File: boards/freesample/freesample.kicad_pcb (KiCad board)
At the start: 8 copper layers, 576 parts, among them J1 SMA, J10 XILINX_JTAG, J11 SMA, J12 SMA, J13 SMA, J14 SMA, J15 SMA, J16 SMA, J17 SMA, J18 SMA, J19 JUMPER, J2 BARREL, J20 JUMPER, J21 JUMPER, J22 SMA, J23 SMA, J24 SMA, J25 SMA, J26 PMOD_HOST, J3 SMA, J4 SMA, J5 SMA, J6 XILINX_JTAG, J7 CONN_INTEGRALSTICK_FPGA_HOST, J8 CONN_INTEGRALSTICK_MCU_HOST, J9 0826-1G1T-23-F, M1 TRACEPAD, M2 LOGO1, M3 LOGO2, M4 LOGO3, M5 LOGO4, M6 LOGO5, M7 LOGO6, Q1 SSM6N58NU, U1 HMC675LP3E, U10 PI6C59S6005, U11 PI6C59S6005, U12 PI6C59S6005, U13 SIP32408, U14 LMK04806, U15 ASG-D-V-A-125.000MHZ, U16 HMC856, U17 NB6L295, U18 PI6C59S6005, U19 NB7V52MMNG, U2 HMC675LP3E, U20 NB7V52MMNG, U21 NB7V52MMNG, U22 PI6C59S6005, U26 MCP1755ST-5002E/MC, U27 LM27761, U28 ADP1763Z-1.0, U29 ADP1763Z-1.0, U3 PI6C59S6005, U30 OKL-T/3-W12P-C, U31 ADP1741, U32 OKL-T/3-W12P-C, U33 ADP1741, U34 ADP1741, U35 OKL-T/3-W12P-C, U36 OKL-T/3-W12P-C, U37 LM27761, U38 OKL-T/3-W12P-C, U39 LM27761, U4 LTC2664CUH-16#PBF, U40 DS25BR150, U41 DS25BR150, U42 ADP1741, U43 ADP1741, U5 TLK10232, U6 LMK61PD0A2, U7 PI6C59S6005, U8 HMC675LP3E, U9 HMC675LP3E

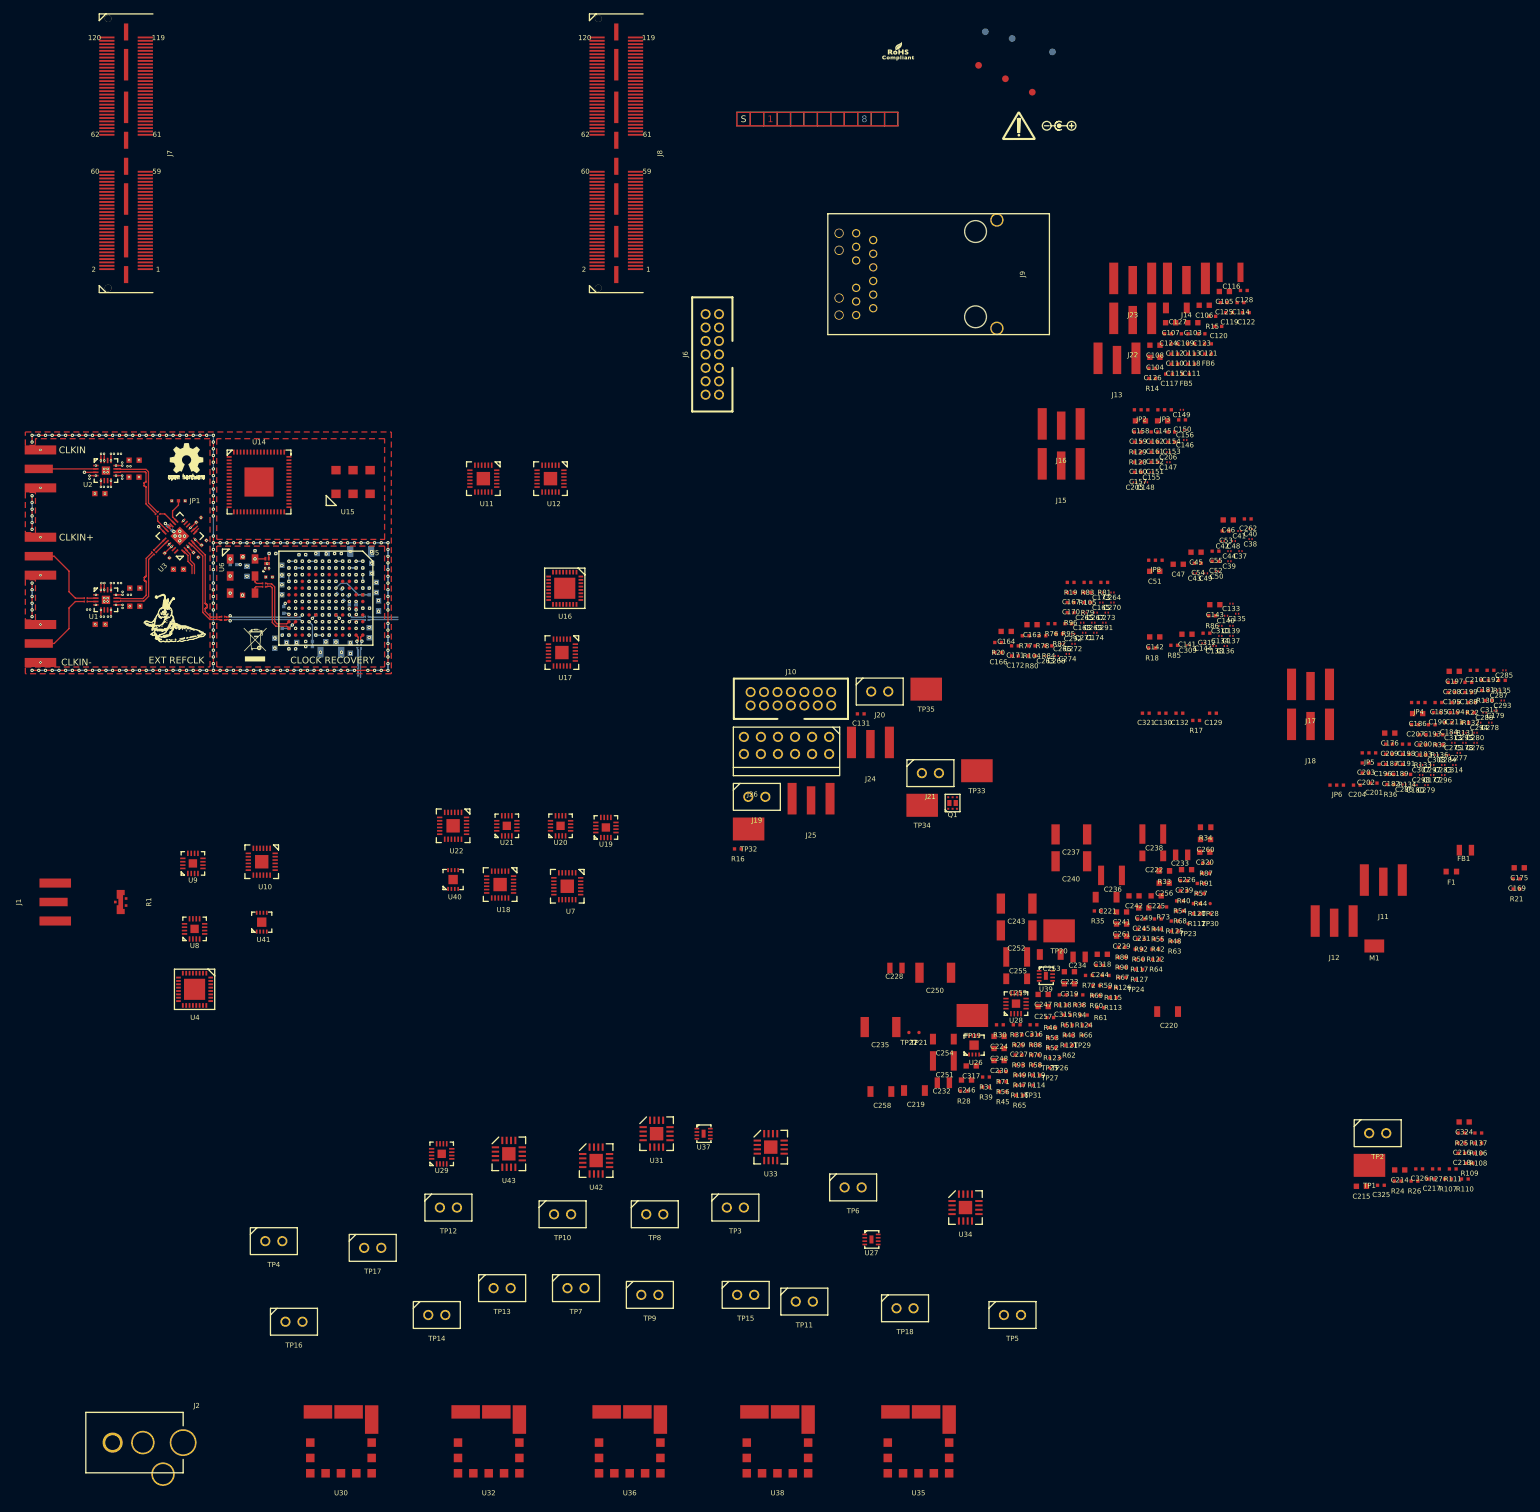
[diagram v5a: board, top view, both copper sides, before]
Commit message: Swapped clock inputs to TLK10232 to reduce via count. Began PLL layout.
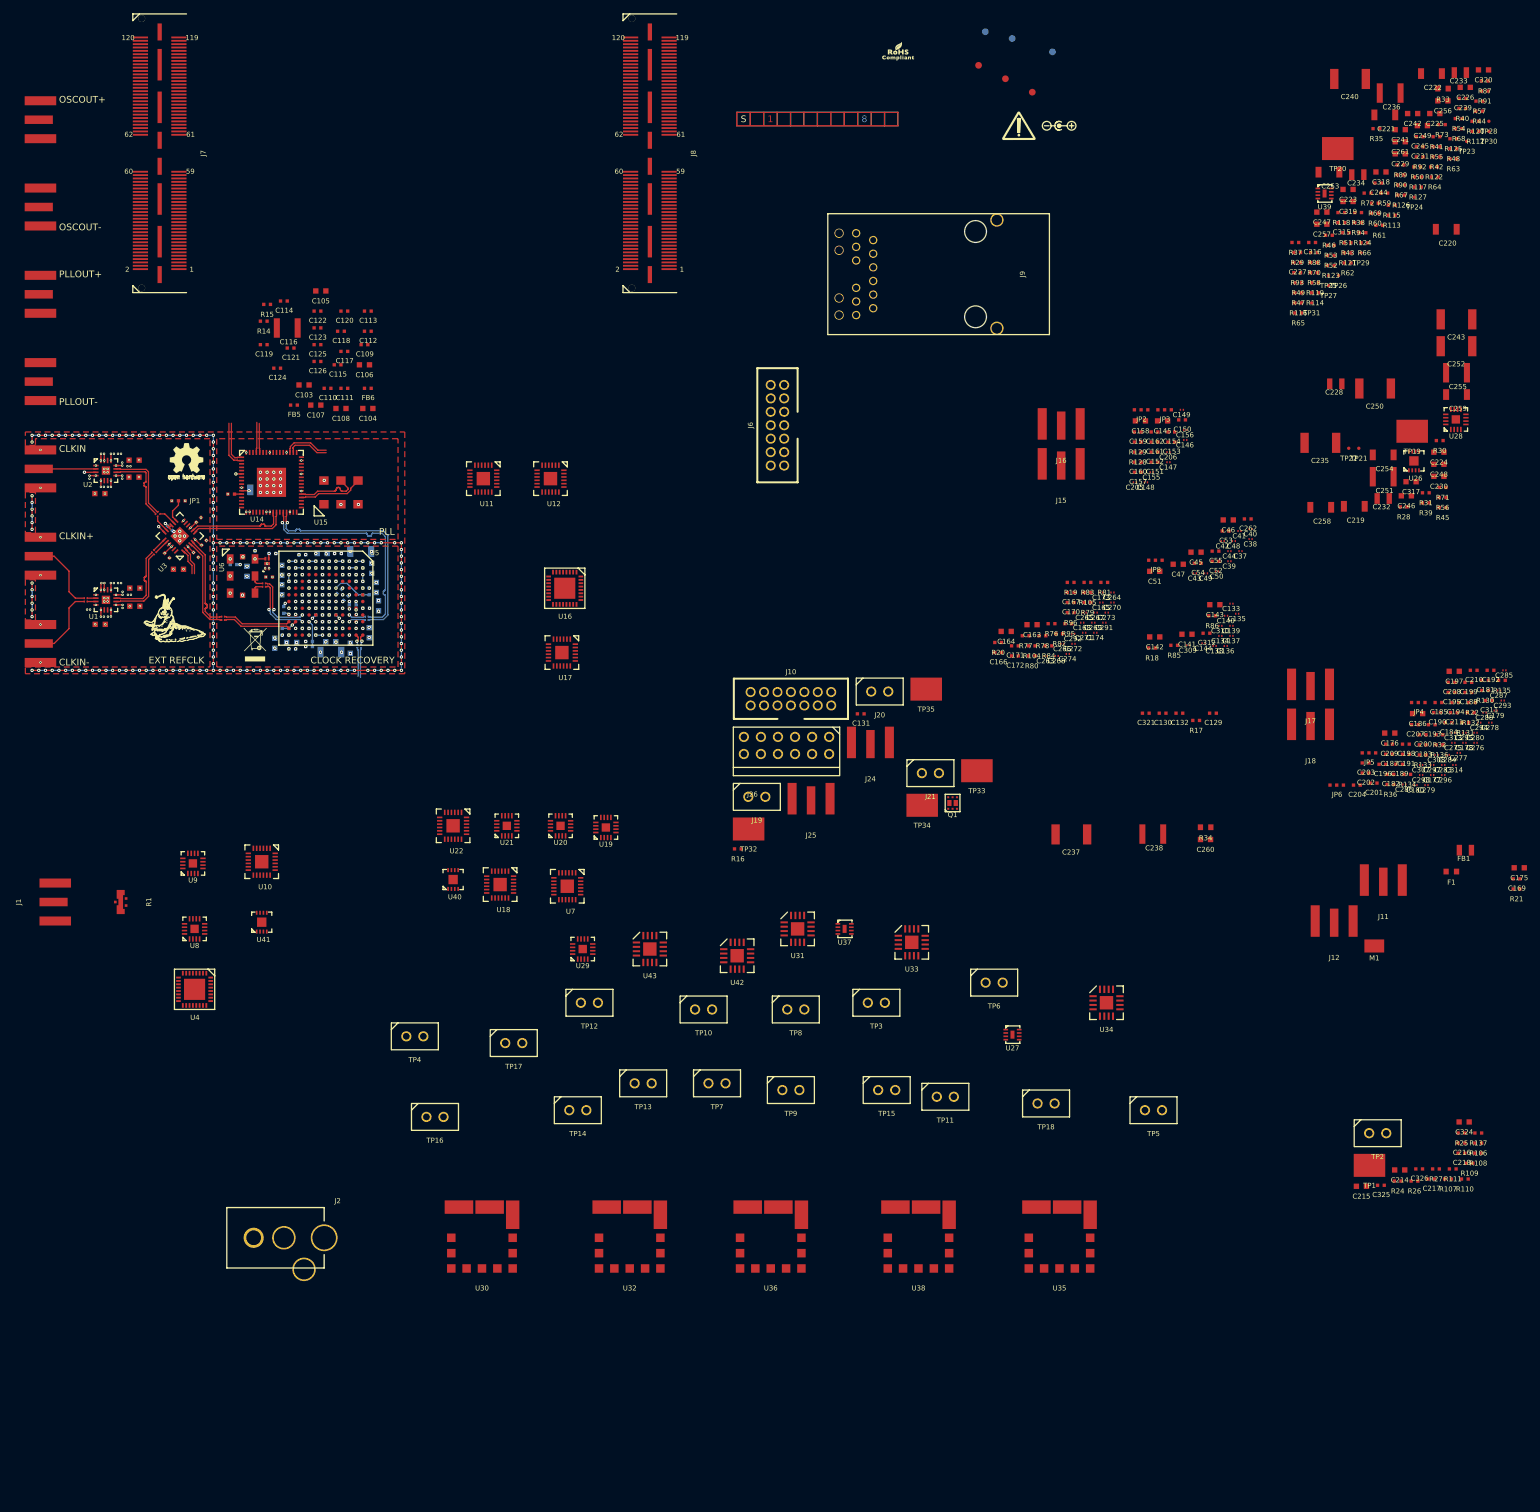
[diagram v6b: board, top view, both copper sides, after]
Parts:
- C127: moved to B.Cu
- moved J14 173.5 mm to (15.9, 112.0), turned to 270 degrees
- moved J22 168.1 mm to (15.9, 73.0), turned to 270 degrees
- moved J23 165.5 mm to (15.9, 86.0), turned to 270 degrees
- moved J13 163.1 mm to (15.9, 99.0), turned to 270 degrees
- moved C128 153.8 mm to (46.6, 128.8)
- moved C119 143.8 mm to (51.5, 106.5)
- moved C114 142.5 mm to (54.5, 100.0)
- moved R15 140.8 mm to (52.0, 100.5)
- moved C116 140.6 mm to (55.0, 104.0)
- moved C127 139.0 mm to (51.0, 128.1), turned to 180 degrees
- moved C122 138.3 mm to (59.5, 101.5)
- moved C121 136.6 mm to (55.5, 107.0)
- moved C125 135.1 mm to (59.5, 106.5)
- moved C105 134.6 mm to (60.0, 98.5)
- moved FB5 132.9 mm to (56.0, 115.5)
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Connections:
- U14 pad 1: /Sample clock muxing/PLL_SAMPCLK_P -> /PLL/PLLOUT_P
- U14 pad 13: /FPGACLK_P -> (no net)
- U14 pad 14: /FPGACLK_N -> (no net)
- U14 pad 19: /PLL/PLLOUT_P -> (no net)
- U14 pad 2: /Sample clock muxing/PLL_SAMPCLK_N -> /PLL/PLLOUT_N
- U14 pad 20: /PLL/PLLOUT_N -> (no net)
- U14 pad 50: (no net) -> /Sample clock muxing/PLL_SAMPCLK_N
- U14 pad 51: (no net) -> /Sample clock muxing/PLL_SAMPCLK_P
- U14 pad 60: (no net) -> /FPGACLK_N
- U14 pad 61: (no net) -> /FPGACLK_P
- U5 pad K10: /CDR/SRC1_AC_N -> /CDR/SRC0_AC_N
- U5 pad K9: /CDR/SRC1_AC_P -> /CDR/SRC0_AC_P
- U5 pad M10: /CDR/SRC0_AC_P -> /CDR/SRC1_AC_P
- U5 pad M11: /CDR/SRC0_AC_N -> /CDR/SRC1_AC_N
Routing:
- net /GND: track 431.5 -> 469.3 mm, vias 289 -> 312
- net /3V3_PLL: track 20.2 -> 56.5 mm, vias 2 -> 15
- net /PLL/CDRCLK_N: track 4.46 -> 33.5 mm, vias 0 -> 1
- net /PLL/CDRCLK_P: track 4.46 -> 33.5 mm, vias 0 -> 1
- net /PLL/EXTCLK_N: track 0.79 -> 14.5 mm
- net /PLL/EXTCLK_P: track 0.94 -> 14.5 mm
- net /PLL/PLL1_CLK_N: track 0.00 -> 9.71 mm
- net /PLL/PLL1_CLK_P: track 0.00 -> 9.68 mm
- net /PLL/PLLOUT_N: track 0.00 -> 6.99 mm
- net /Sample clock muxing/PLL_SAMPCLK_P: track 0.00 -> 6.92 mm
- net /OSC_PWR_EN: track 7.95 -> 1.15 mm
- net /PLL/PLLOUT_P: track 0.00 -> 6.38 mm
- net /Sample clock muxing/PLL_SAMPCLK_N: track 0.00 -> 6.32 mm
- net /FPGACLK_P: track 0.00 -> 4.50 mm
- net /FPGACLK_N: track 0.00 -> 4.35 mm
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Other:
- board text added: "OSCOUT+"
- board text added: "OSCOUT-"
- board text added: "PLL"
- board text added: "PLLOUT+"
- board text added: "PLLOUT-"

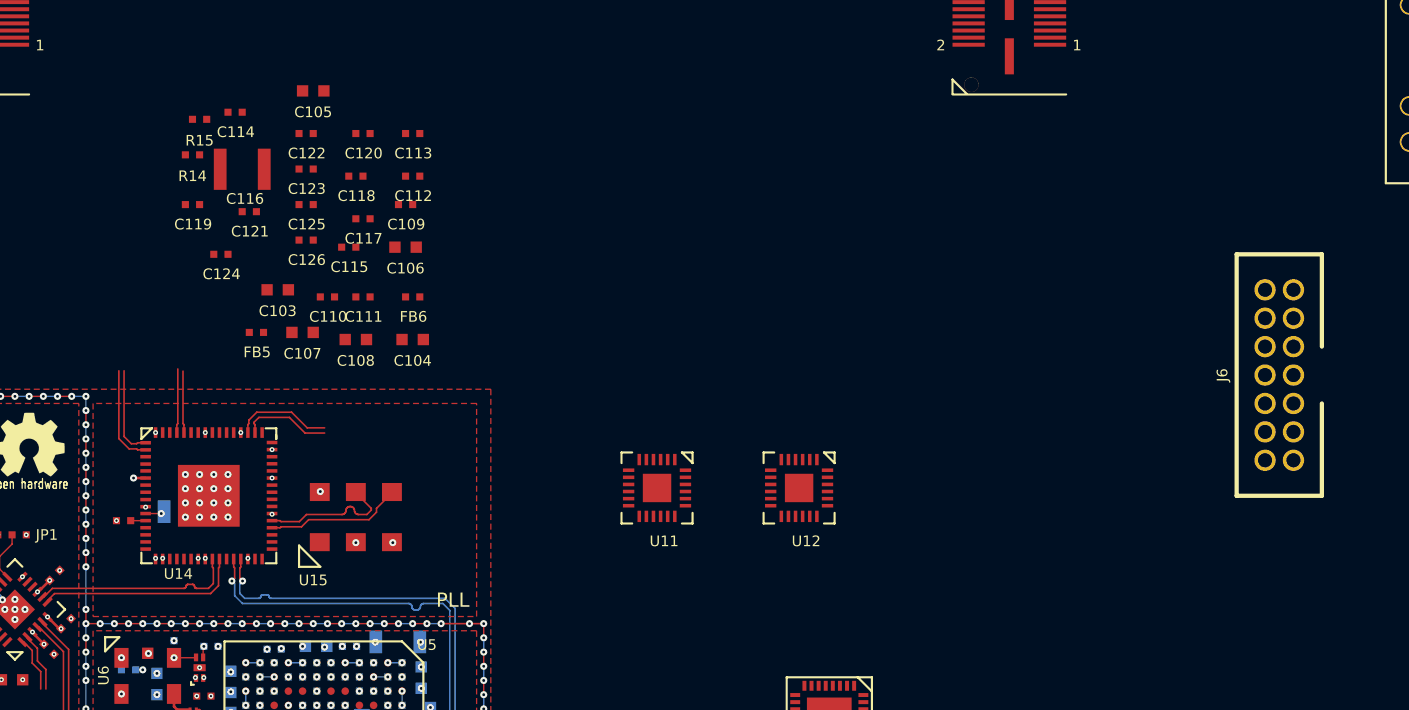
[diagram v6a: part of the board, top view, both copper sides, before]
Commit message: Finished initial PLL layout
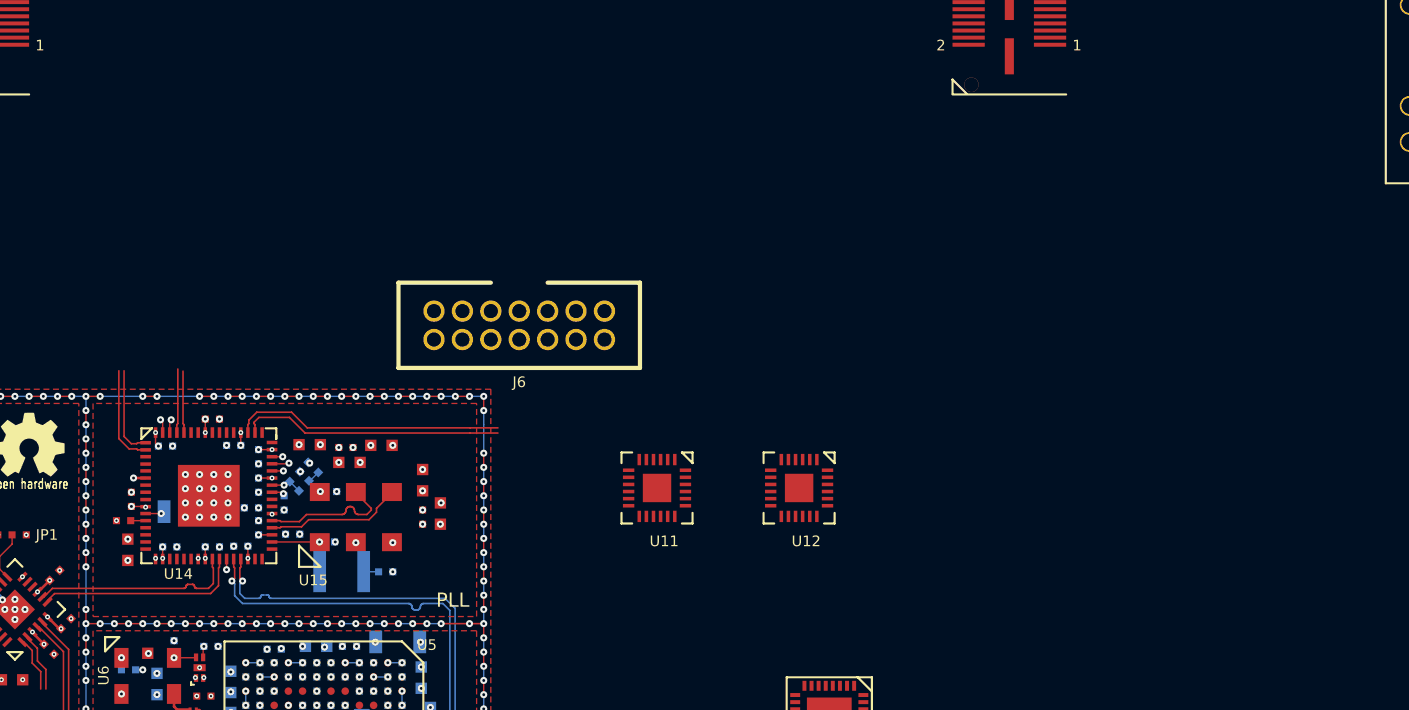
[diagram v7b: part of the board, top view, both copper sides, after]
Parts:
- C109, C110, C111, C112, C113, C114, C115, C116, C118, C119, C120, C121, C122, C123, C124, C126, R14, R15: moved to B.Cu
- moved J6 53.6 mm to (74.5, 115.0), turned to 180 degrees
- moved C105 34.8 mm to (47.0, 130.8), turned to 90 degrees
- moved R14 32.3 mm to (65.1, 132.3)
- moved C113 32.3 mm to (52.9, 130.6)
- moved C112 31.2 mm to (49.9, 130.6)
- moved C114 30.9 mm to (61.0, 130.2)
- moved C122 29.4 mm to (54.9, 130.6), turned to 180 degrees
- moved C116 29.2 mm to (62.0, 132.3)
- moved R15 25.8 mm to (60.0, 125.0), turned to 135 degrees
- moved C109 24.5 mm to (58.5, 129.7)
- moved C118 24.5 mm to (55.6, 127.8), turned to 180 degrees
- moved C125 24.1 mm to (47.2, 127.2), turned to 90 degrees
- moved C120 23.9 mm to (56.1, 124.2), turned to 270 degrees
- moved C123 21.9 mm to (49.6, 123.5)
- moved C119 20.5 mm to (58.7, 125.7), turned to 45 degrees
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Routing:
- net /GND: track 469.3 -> 565.4 mm, vias 312 -> 373
- net /3V3_PLL: track 56.5 -> 93.6 mm, vias 15 -> 32
- net /OSC_PWR_EN: track 1.15 -> 26.4 mm
- net /SERDES_MDC: track 12.4 -> 33.6 mm
- net /SERDES_MDIO: track 11.6 -> 31.9 mm
- net /SERDES_RST_N: track 9.81 -> 29.6 mm
- net /SERDES_MODE_SEL: track 14.5 -> 34.0 mm
- net /CDR/SERDES_TCK: track 13.1 -> 32.0 mm
- net /PLL_HOLDOVER: track 0.00 -> 18.0 mm, vias 0 -> 1
- net /CDR/SERDES_TDO: track 3.61 -> 21.1 mm
- net /CDR/SERDES_TDI: track 12.2 -> 29.5 mm
- net /CDR/SERDES_TMS: track 12.4 -> 29.3 mm
- net /SERDES_POWER_EN: track 11.8 -> 28.5 mm
- net /OSC_OS: track 11.0 -> 27.1 mm
- net /OSC_FS0: track 13.7 -> 29.7 mm
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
